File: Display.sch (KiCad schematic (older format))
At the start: 16 parts, among them Q1 Q_NPN_BCE, Q2 Q_NPN_BCE, U1 74LS47, U5 DA56-11GWA

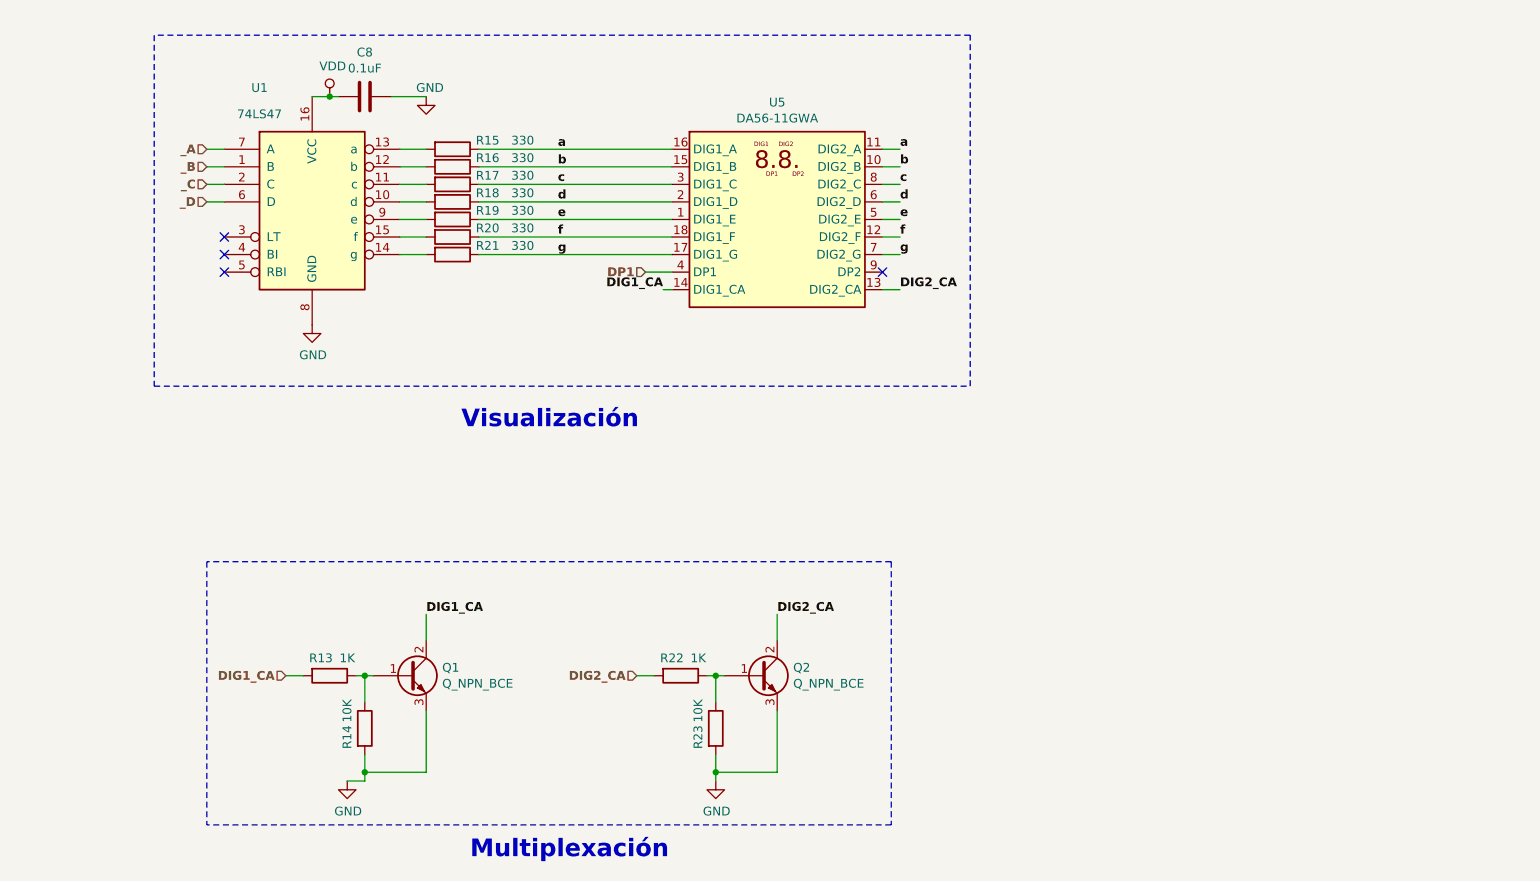
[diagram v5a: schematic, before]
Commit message: Se agrega info del circuito,prolijidad en conexiones  se corrije,ERC Warninsg no errores,pendinete Datasheet y algunos numeros de parte,Comentario esquematico1: no es necesario con los labels que esta considero que esta ok, componentes los dejo en 0603, grilla en pcb 0.127 mm a criterio propio, se colocan fiduciales, pendiente lo demas de PCB.
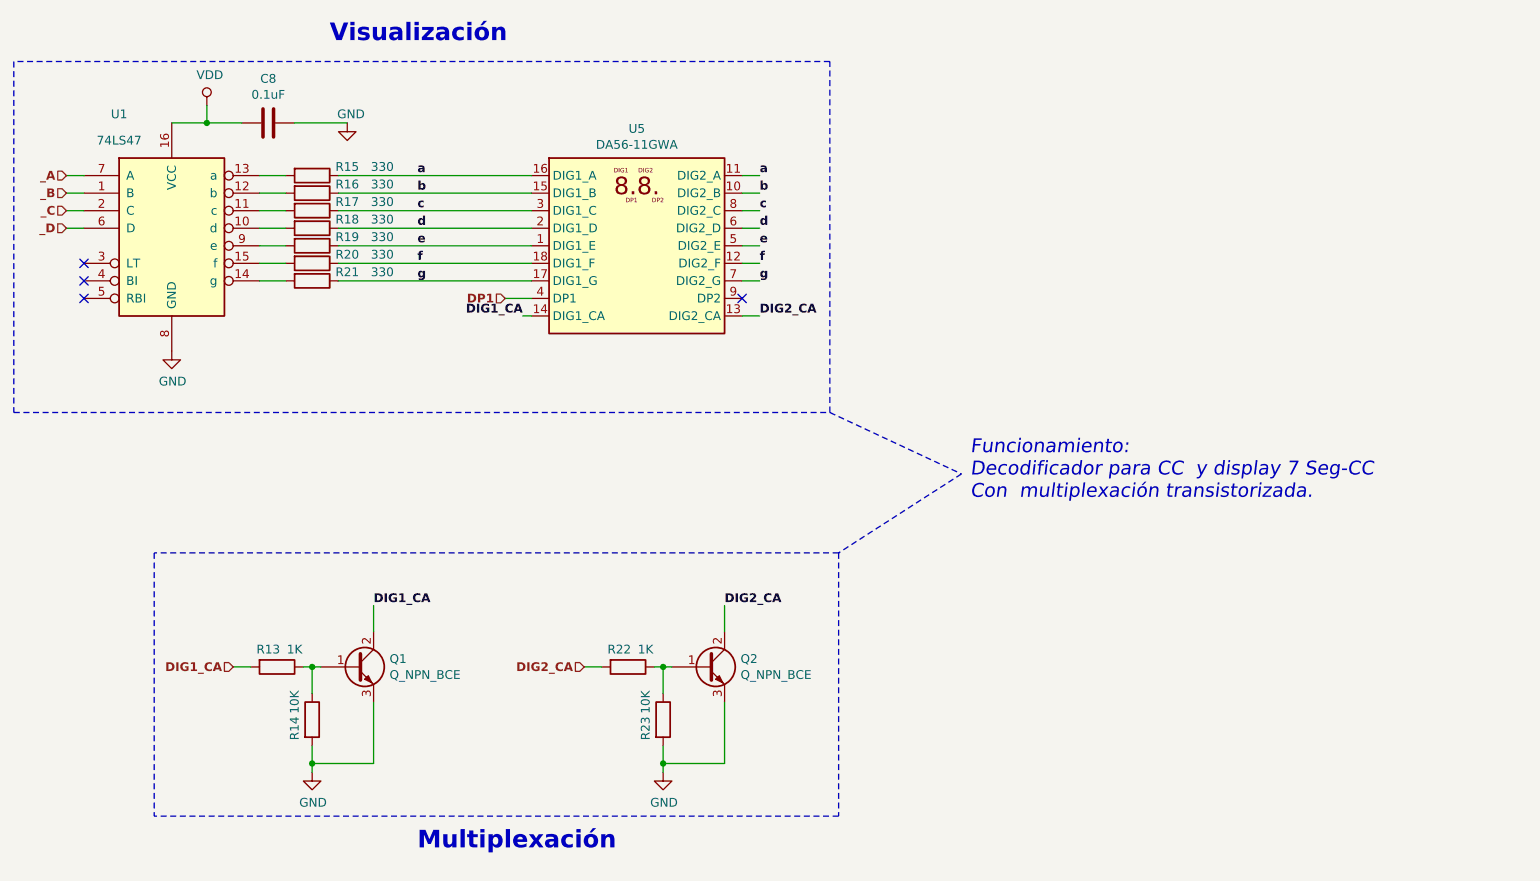
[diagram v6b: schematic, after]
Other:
- note added: "Funcionamiento:\nDecodificador para CC y display 7 Seg-CC\nCon multiplexación transistorizada."
- moved on the sheet: C8, Q1, Q2, R13, R14, R15, R16, R17, R18, R19, R20, R21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

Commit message: TP Finalizado
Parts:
- C8:  Part Number (none) -> 399-1282-2-ND
- Q1, Q2: value Q_NPN_BCE -> STR1550;  Part Number (none) -> 497-13847-6-ND
- R13, R22:  Part Number (none) -> P1.00KHDKR-ND
- R14, R23:  Part Number (none) -> 1276-3485-2-ND
- R15, R16, R17, R18, R19, R20, R21:  Part Number (none) -> RHM330AZCT-ND
- U1:  Part Number (none) -> 296-3712-5-ND
- U5:  Part Number (none) -> 604-DA56-11CGKWA
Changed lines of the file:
@@
 F 2 "Package_DIP:DIP-16_W7.62mm" H 3550 2500 50  0001 C CNN
 F 3 "http://www.ti.com/lit/gpn/sn74LS47" H 3550 2500 50  0001 C CNN
+F 4 "296-3712-5-ND" H 3550 2500 50  0001 C CNN " Part Number"
 	1    3550 2500
 	1    0    0    -1
@@
 F 2 "Display_7Segment:DA56-11CGKWA" H 6220 1950 50  0001 C CNN
 F 3 "http://www.kingbrightusa.com/images/catalog/SPEC/DA56-11GWA.pdf" H 6080 2700 50  0001 C CNN
+F 4 "604-DA56-11CGKWA" H 6200 2600 50  0001 C CNN " Part Number"
 	1    6200 2600
 	1    0    0    -1
@@
 F 1 "330" V 4300 2600 50  0000 C CNN
 F 2 "Resistor_SMD:R_0603_1608Metric_Pad1.05x0.95mm_HandSolder" V 4280 2200 50  0001 C CNN
-F 3 "~" H 4350 2200 50  0001 C CNN
+F 3 "https://www.rohm.com/datasheet/KTR03EZPF/ktr-e" H 4350 2200 50  0001 C CNN
+F 4 "RHM330AZCT-ND" H 4350 2200 50  0001 C CNN " Part Number"
 	1    4350 2200
 	0    1    1    0
@@
 F 1 "330" V 4300 2700 50  0000 C CNN
 F 2 "Resistor_SMD:R_0603_1608Metric_Pad1.05x0.95mm_HandSolder" V 4280 2300 50  0001 C CNN
-F 3 "~" H 4350 2300 50  0001 C CNN
+F 3 "https://www.rohm.com/datasheet/KTR03EZPF/ktr-e" H 4350 2300 50  0001 C CNN
+F 4 "RHM330AZCT-ND" H 4350 2300 50  0001 C CNN " Part Number"
 	1    4350 2300
 	0    1    1    0
@@
 F 1 "330" V 4300 2800 50  0000 C CNN
 F 2 "Resistor_SMD:R_0603_1608Metric_Pad1.05x0.95mm_HandSolder" V 4280 2400 50  0001 C CNN
-F 3 "~" H 4350 2400 50  0001 C CNN
+F 3 "https://www.rohm.com/datasheet/KTR03EZPF/ktr-e" H 4350 2400 50  0001 C CNN
+F 4 "RHM330AZCT-ND" H 4350 2400 50  0001 C CNN " Part Number"
 	1    4350 2400
 	0    1    1    0
@@
 F 1 "330" V 4300 2900 50  0000 C CNN
 F 2 "Resistor_SMD:R_0603_1608Metric_Pad1.05x0.95mm_HandSolder" V 4280 2500 50  0001 C CNN
-F 3 "~" H 4350 2500 50  0001 C CNN
+F 3 "https://www.rohm.com/datasheet/KTR03EZPF/ktr-e" H 4350 2500 50  0001 C CNN
+F 4 "RHM330AZCT-ND" H 4350 2500 50  0001 C CNN " Part Number"
 	1    4350 2500
 	0    1    1    0
@@
 F 1 "330" V 4300 3000 50  0000 C CNN
 F 2 "Resistor_SMD:R_0603_1608Metric_Pad1.05x0.95mm_HandSolder" V 4280 2600 50  0001 C CNN
-F 3 "~" H 4350 2600 50  0001 C CNN
+F 3 "https://www.rohm.com/datasheet/KTR03EZPF/ktr-e" H 4350 2600 50  0001 C CNN
+F 4 "RHM330AZCT-ND" H 4350 2600 50  0001 C CNN " Part Number"
 	1    4350 2600
 	0    1    1    0
@@
 F 1 "330" V 4300 3100 50  0000 C CNN
 F 2 "Resistor_SMD:R_0603_1608Metric_Pad1.05x0.95mm_HandSolder" V 4280 2700 50  0001 C CNN
-F 3 "~" H 4350 2700 50  0001 C CNN
+F 3 "https://www.rohm.com/datasheet/KTR03EZPF/ktr-e" H 4350 2700 50  0001 C CNN
+F 4 "RHM330AZCT-ND" H 4350 2700 50  0001 C CNN " Part Number"
 	1    4350 2700
 	0    1    1    0
@@
 F 1 "330" V 4300 3200 50  0000 C CNN
 F 2 "Resistor_SMD:R_0603_1608Metric_Pad1.05x0.95mm_HandSolder" V 4280 2800 50  0001 C CNN
-F 3 "~" H 4350 2800 50  0001 C CNN
+F 3 "https://www.rohm.com/datasheet/KTR03EZPF/ktr-e" H 4350 2800 50  0001 C CNN
+F 4 "RHM330AZCT-ND" H 4350 2800 50  0001 C CNN " Part Number"
 	1    4350 2800
 	0    1    1    0
@@
 F 1 "0.1uF" V 3939 1900 50  0000 C CNN
 F 2 "Capacitor_SMD:C_0603_1608Metric" H 4138 1750 50  0001 C CNN
-F 3 "~" H 4100 1900 50  0001 C CNN
+F 3 "https://content.kemet.com/datasheets/KEM_C1002_X7R_SMD.pdf" H 4100 1900 50  0001 C CNN
 F 4 "732-7939-1-ND" V 4100 1900 50  0001 C CNN "PArt Number"
+F 5 "399-1282-2-ND" H 4100 1900 50  0001 C CNN " Part Number"
 	1    4100 1900
 	0    1    1    0
@@
 F 1 "10K" V 4250 5400 50  0000 C CNN
 F 2 "Resistor_SMD:R_0603_1608Metric_Pad1.05x0.95mm_HandSolder" V 4280 5300 50  0001 C CNN
-F 3 "~" H 4350 5300 50  0001 C CNN
+F 3 "http://www.samsungsem.com/kr/support/product-search/chip-resistor/__icsFiles/afieldfile/2019/01/21/RC_Spec_Sheet(1901).pdf" H 4350 5300 50  0001 C CNN
+F 4 "1276-3485-2-ND" H 4350 5300 50  0001 C CNN " Part Number"
 	1    4350 5300
 	1    0    0    -1
@@
 F 1 "1K" V 4050 5100 50  0000 C CNN
 F 2 "Resistor_SMD:R_0603_1608Metric_Pad1.05x0.95mm_HandSolder" V 4080 5000 50  0001 C CNN
-F 3 "~" H 4150 5000 50  0001 C CNN
+F 3 "https://industrial.panasonic.com/cdbs/www-data/pdf/RDA0000/AOA0000C304.pdf" H 4150 5000 50  0001 C CNN
+F 4 "P1.00KHDKR-ND" H 4150 5000 50  0001 C CNN " Part Number"
 	1    4150 5000
 	0    1    1    0
@@
 AR Path="/5D021BAF/5CD2B4DB" Ref="Q?"  Part="1"
 F 0 "Q1" H 4791 5046 50  0000 L CNN
-F 1 "Q_NPN_BCE" H 4791 4955 50  0000 L CNN
+F 1 "STR1550" H 4791 4955 50  0000 L CNN
 F 2 "Package_TO_SOT_SMD:SOT-23" H 4800 5100 50  0001 C CNN
-F 3 "~" H 4600 5000 50  0001 C CNN
+F 3 "https://www.st.com/content/ccc/resource/technical/document/datasheet/1d/0e/46/c1/5b/ea/4a/28/DM00040355.pdf/files/DM00040355.pdf/jcr:content/translations/en.DM00040355.pdf" H 4600 5000 50  0001 C CNN
+F 4 "497-13847-6-ND" H 4600 5000 50  0001 C CNN " Part Number"
 	1    4600 5000
 	1    0    0    -1
@@
 F 1 "10K" V 6250 5400 50  0000 C CNN
 F 2 "Resistor_SMD:R_0603_1608Metric_Pad1.05x0.95mm_HandSolder" V 6280 5300 50  0001 C CNN
-F 3 "~" H 6350 5300 50  0001 C CNN
+F 3 "http://www.samsungsem.com/kr/support/product-search/chip-resistor/__icsFiles/afieldfile/2019/01/21/RC_Spec_Sheet(1901).pdf" H 6350 5300 50  0001 C CNN
+F 4 "1276-3485-2-ND" H 6350 5300 50  0001 C CNN " Part Number"
 	1    6350 5300
 	1    0    0    -1
@@
 F 1 "1K" V 6050 5100 50  0000 C CNN
 F 2 "Resistor_SMD:R_0603_1608Metric_Pad1.05x0.95mm_HandSolder" V 6080 5000 50  0001 C CNN
-F 3 "~" H 6150 5000 50  0001 C CNN
+F 3 "https://industrial.panasonic.com/cdbs/www-data/pdf/RDA0000/AOA0000C304.pdf" H 6150 5000 50  0001 C CNN
+F 4 "P1.00KHDKR-ND" H 6150 5000 50  0001 C CNN " Part Number"
 	1    6150 5000
 	0    1    1    0
@@
 AR Path="/5D021BAF/5CDFE125" Ref="Q?"  Part="1"
 F 0 "Q2" H 6791 5046 50  0000 L CNN
-F 1 "Q_NPN_BCE" H 6791 4955 50  0000 L CNN
+F 1 "STR1550" H 6791 4955 50  0000 L CNN
 F 2 "Package_TO_SOT_SMD:SOT-23" H 6800 5100 50  0001 C CNN
-F 3 "~" H 6600 5000 50  0001 C CNN
+F 3 "https://www.st.com/content/ccc/resource/technical/document/datasheet/1d/0e/46/c1/5b/ea/4a/28/DM00040355.pdf/files/DM00040355.pdf/jcr:content/translations/en.DM00040355.pdf" H 6600 5000 50  0001 C CNN
+F 4 "497-13847-6-ND" H 6600 5000 50  0001 C CNN " Part Number"
 	1    6600 5000
 	1    0    0    -1
